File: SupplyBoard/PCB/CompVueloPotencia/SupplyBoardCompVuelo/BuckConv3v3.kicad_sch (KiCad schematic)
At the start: 11 parts, among them U2 TPS5430DDA

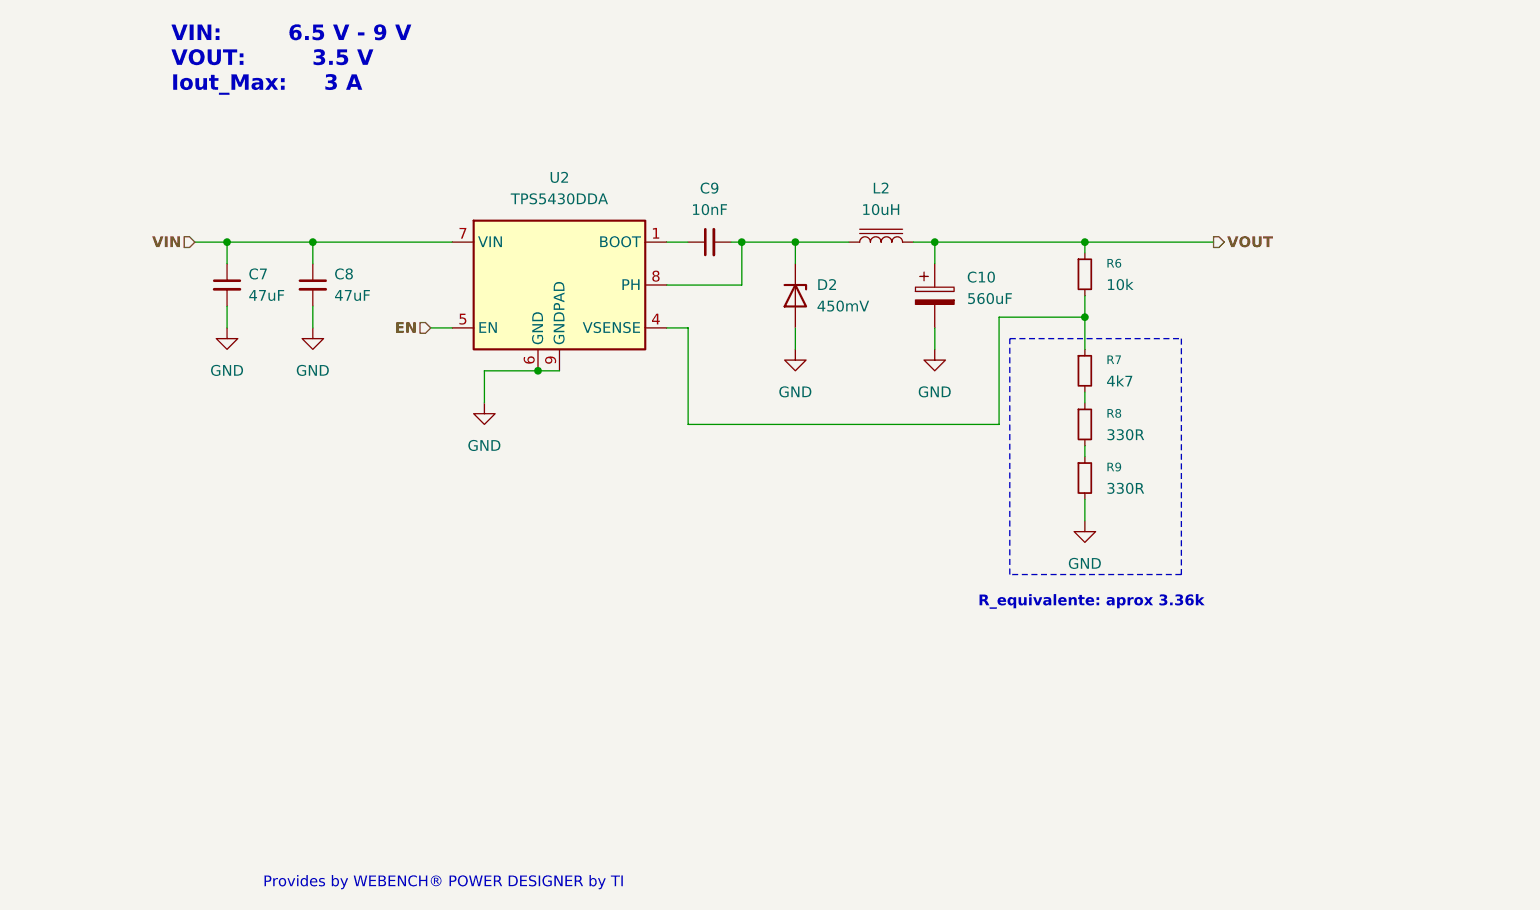
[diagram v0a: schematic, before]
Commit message: Supply Board - Remake Schematic in KiCad 9
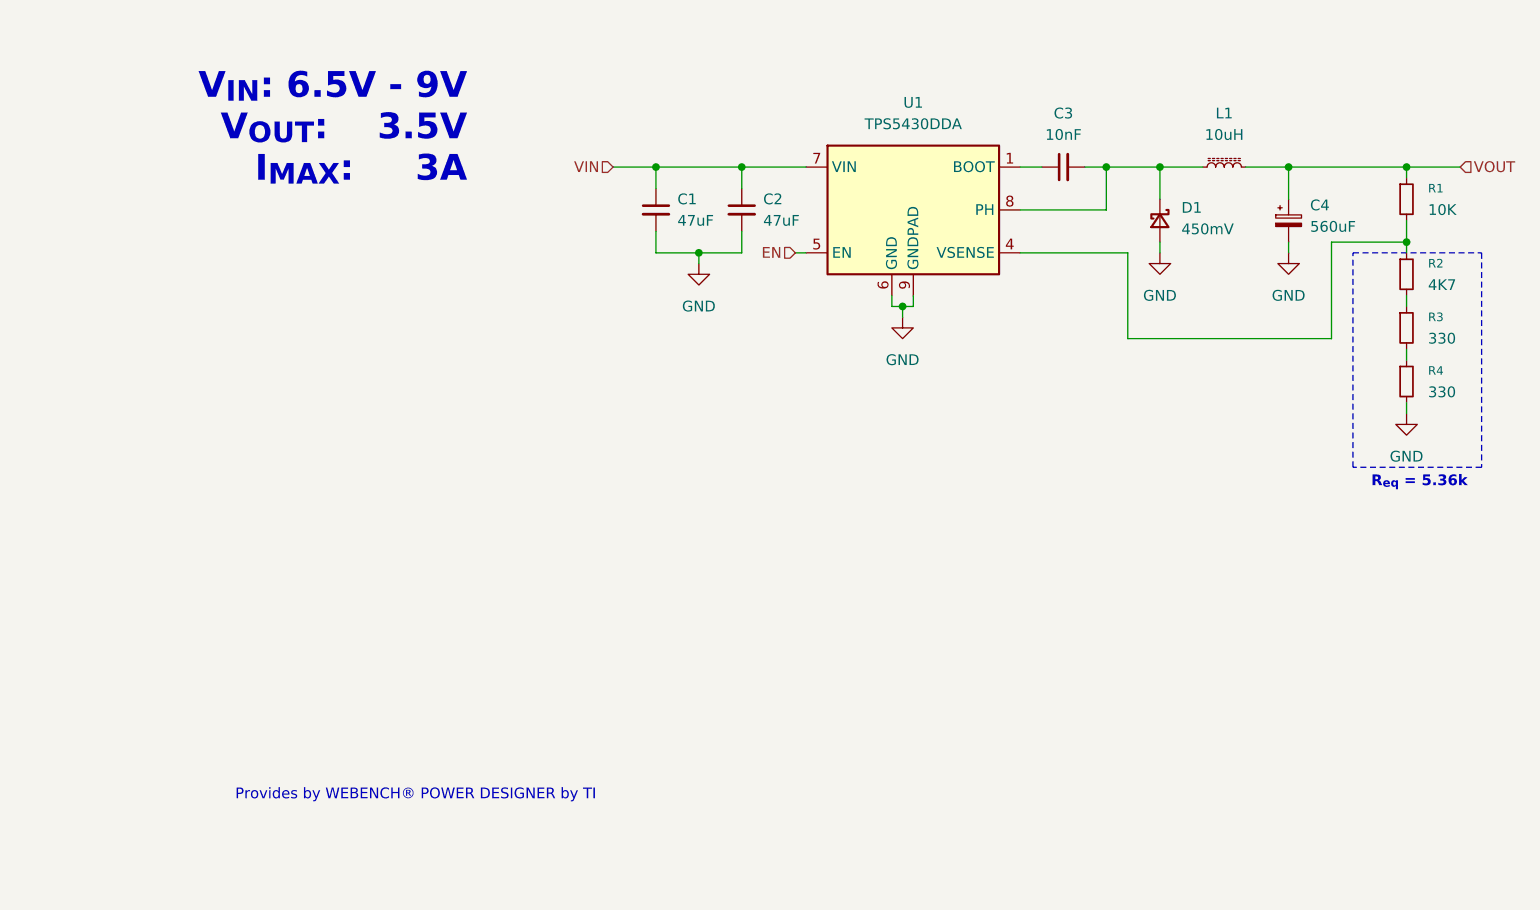
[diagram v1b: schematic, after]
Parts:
- removed C10: 560uF, Capacitor_SMD:C_0805_2012Metric, symbol Device:C_Polarized
- removed C7, C8: 47uF, Capacitor_SMD:C_0805_2012Metric, symbol Device:C_Small
- removed C9: 10nF, Capacitor_SMD:C_0805_2012Metric, symbol Device:C_Small
- removed D2: 450mV, Capacitor_SMD:C_0805_2012Metric, symbol Device:D_Zener
- removed L2: 10uH, Inductor_SMD:L_Sumida_CDMC6D28_7.25x6.5mm, symbol Device:L_Iron
- removed R6: 10k, Resistor_SMD:R_0805_2012Metric, symbol Device:R_Small
- removed R7: 4k7, Resistor_SMD:R_0805_2012Metric, symbol Device:R_Small
- removed R8, R9: 330R, Resistor_SMD:R_0805_2012Metric, symbol Device:R_Small
- removed U2: TPS5430DDA, Package_SO:TI_SO-PowerPAD-8_ThermalVias, symbol Regulator_Switching:TPS5430DDA
- added C1, C2: 47uF, symbol Device:C_Small
- added C3: 10nF, symbol Device:C_Small
- added C4: 560uF, symbol Device:C_Polarized_Small
- added D1: 450mV, symbol Device:D_Schottky_Small
- added L1: 10uH, symbol Device:L_Ferrite_Small
- added R1: 10K, symbol Device:R_Small
- added R2: 4K7, symbol Device:R_Small
- added R3, R4: 330, symbol Device:R_Small
- added U1: TPS5430DDA, Package_SO:TI_SO-PowerPAD-8_ThermalVias, symbol Regulator_Switching:TPS5430DDA
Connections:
- net EN: now also U1.5 (EN)
- net GND: now also C1.2, C2.2, C4.2, D1.2 (A), R4.2, U1.6 (GND), U1.9 (GNDPAD)
- net VIN: now also C1.1, C2.1, U1.7 (VIN)
- net VOUT: now also C4.1, L1.2, R1.1
- new net: R1.2, R2.1, U1.4 (VSENSE)
- new net: R2.2, R3.1
- new net: R3.2, R4.1
- new net: C3.2, D1.1 (K), L1.1, U1.8 (PH)
- new net: C3.1, U1.1 (BOOT)
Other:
- note added: "R_{eq} = 5.36k"
- note added: "V_{IN}: 6.5V - 9V V_{OUT}: 3.5V I_{MAX}: 3A"
- note removed: "R_equivalente: aprox 3.36k"
- note removed: "VIN: 6.5 V - 9 V VOUT: 3.5 V Iout_Max: 3 A"
- company: XIMBAL EK ELECTRONICA -> (none)
